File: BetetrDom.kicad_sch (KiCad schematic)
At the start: 8 parts, among them J1 XT60PW-M, J2 Raspberry_Pi_2_3

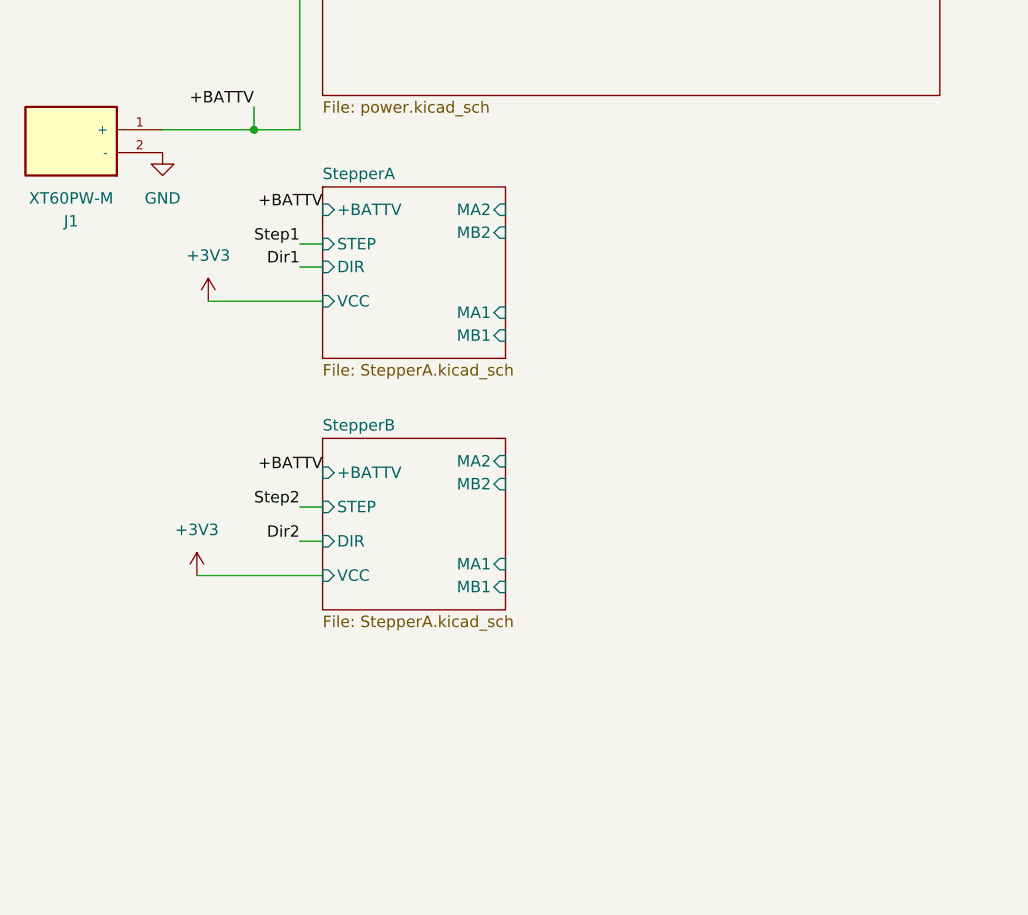
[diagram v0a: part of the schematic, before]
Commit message: with ports for steppers
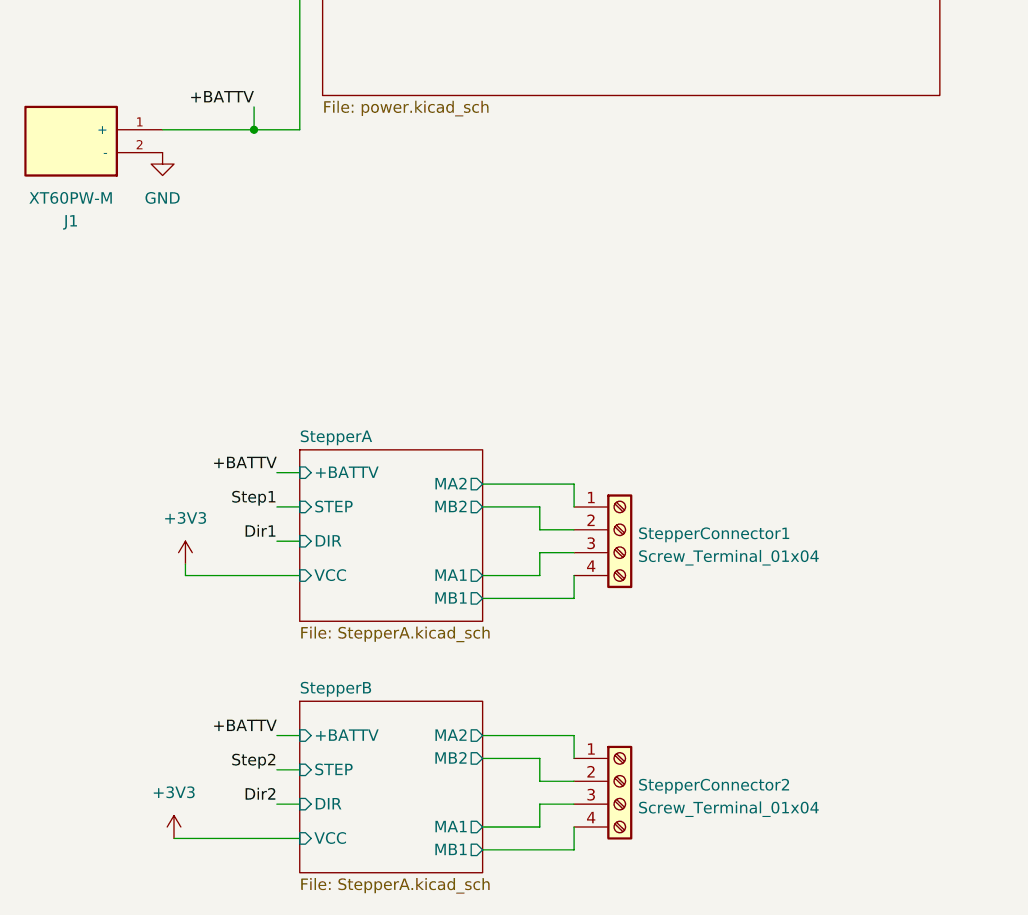
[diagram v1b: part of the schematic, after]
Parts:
- added StepperConnector1, StepperConnector2: Screw_Terminal_01x04, TerminalBlock_TE-Connectivity:TerminalBlock_TE_282834-4_1x04_P2.54mm_Horizontal, symbol Connector:Screw_Terminal_01x04
- J1: footprint AMASS_XT60PW-M -> iclr:AMASS_XT60PW-M
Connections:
- net StepperA/MA1: now also StepperConnector1.3 (Pin_3)
- net StepperA/MA2: now also StepperConnector1.1 (Pin_1)
- net StepperA/MB1: now also StepperConnector1.4 (Pin_4)
- net StepperA/MB2: now also StepperConnector1.2 (Pin_2)
- net StepperB/MA1: now also StepperConnector2.3 (Pin_3)
- net StepperB/MA2: now also StepperConnector2.1 (Pin_1)
- net StepperB/MB1: now also StepperConnector2.4 (Pin_4)
- net StepperB/MB2: now also StepperConnector2.2 (Pin_2)

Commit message: added zener diodes
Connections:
- net ID_SCL_EEPROM: no longer names the net of J2.28 (ID_SC/GPIO1)
- net ID_SCL_EEPROM: now also J2.27 (ID_SD/GPIO0); no longer TP6.1
- net ID_SDA_EEPROM: no longer names the net of TP5.1
- net ID_SDA_EEPROM: no longer J2.27 (ID_SD/GPIO0)
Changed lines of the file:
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@@
+	(wire
+		(pts
+			(xy 194.31 77.47) (xy 194.31 80.01)
+		)
+		(stroke
+			(width 0)
+			(type default)
+		)
+	)
 	(wire
 		(pts
@@
 	(wire
 		(pts
-			(xy 194.31 77.47) (xy 213.36 77.47)
-		)
-		(stroke
-			(width 0)
-			(type default)
-		)
-	)
-	(wire
-		(pts
 			(xy 177.8 67.31) (xy 179.07 67.31)
 		)
@@
 	(wire
 		(pts
-			(xy 194.31 80.01) (xy 213.36 80.01)
-		)
-		(stroke
-			(width 0)
-			(type default)
-		)
-	)
-	(wire
-		(pts
 			(xy 73.66 104.14) (xy 77.47 104.14)
 		)
@@
 			(width 0)
 			(type default)
-		)
-	)
-	(label "ID_SCL_EEPROM"
-		(at 196.85 80.01 0)
-		(fields_autoplaced yes)
-		(effects
-			(font
-				(size 1.27 1.27)
-			)
-			(justify left bottom)
 		)
 	)
@@
 		)
 	)
-	(label "ID_SDA_EEPROM"
-		(at 196.85 77.47 0)
-		(fields_autoplaced yes)
-		(effects
-			(font
-				(size 1.27 1.27)
-			)
-			(justify left bottom)
-		)
-	)

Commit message: UPDATE
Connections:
- net at J2.27 (ID_SD/GPIO0), J2.28 (ID_SC/GPIO1): now also TP5.1, TP6.1
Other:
- moved on the sheet: TP5, TP6
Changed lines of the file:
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@@
 	(paper "A4")
+	(junction
+		(at 194.31 77.47)
+		(diameter 0)
+		(color 0 0 0 0)
+	)
 	(junction
 		(at 179.07 133.35)
@@
 	(junction
 		(at 41.91 59.69)
+		(diameter 0)
+		(color 0 0 0 0)
+	)
+	(junction
+		(at 194.31 80.01)
 		(diameter 0)
 		(color 0 0 0 0)
@@
 	(symbol
 		(lib_id "Connector:TestPoint")
-		(at 213.36 80.01 270)
+		(at 194.31 80.01 270)
 		(unit 1)
 		(exclude_from_sim no)
@@
 		(fields_autoplaced yes)
 		(property "Reference" "TP6"
-			(at 218.059 79.1753 90)
+			(at 199.009 79.1753 90)
 			(effects
 				(font
@@
 		)
 		(property "Value" "SCL_EEPROM"
-			(at 218.059 81.7122 90)
+			(at 199.009 81.7122 90)
 			(effects
 				(font
@@
 		)
 		(property "Footprint" "TestPoint:TestPoint_Pad_1.5x1.5mm"
-			(at 213.36 85.09 0)
+			(at 194.31 85.09 0)
 			(effects
 				(font
@@
 		)
 		(property "Datasheet" "~"
-			(at 213.36 85.09 0)
+			(at 194.31 85.09 0)
 			(effects
 				(font
@@
 		)
 		(property "Description" ""
-			(at 213.36 80.01 0)
+			(at 194.31 80.01 0)
 			(effects
 				(font
@@
 	(symbol
 		(lib_id "Connector:TestPoint")
-		(at 213.36 77.47 270)
+		(at 194.31 77.47 270)
 		(unit 1)
 		(exclude_from_sim no)
@@
 		(fields_autoplaced yes)
 		(property "Reference" "TP5"
-			(at 218.059 76.6353 90)
+			(at 199.009 76.6353 90)
 			(effects
 				(font
@@
 		)
 		(property "Value" "SDA_EEPROM"
-			(at 218.059 79.1722 90)
+			(at 199.009 79.1722 90)
 			(effects
 				(font
@@
 		)
 		(property "Footprint" "TestPoint:TestPoint_Pad_1.5x1.5mm"
-			(at 213.36 82.55 0)
+			(at 194.31 82.55 0)
 			(effects
 				(font
@@
 		)
 		(property "Datasheet" "~"
-			(at 213.36 82.55 0)
+			(at 194.31 82.55 0)
 			(effects
 				(font
@@
 		)
 		(property "Description" ""
-			(at 213.36 77.47 0)
-			(effects
-				(font
+			(at 194.31 77.47 0)
+			(effects
+				(font

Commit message: finished pcb layouts, ready for check p sure
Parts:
- added C5: 0.1uF, Capacitor_SMD:C_0402_1005Metric, symbol Device:C_Small
- added H1, H2, H3, H4: MountingHole_Pad, MountingHole:MountingHole_3.2mm_M3_DIN965_Pad, symbol Mechanical:MountingHole_Pad
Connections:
- net GND: now also C5.2, H1.1, H2.1, H3.1, H4.1; no longer J1.2 (-)
- net StepperA/MA1: now also StepperConnector1.2 (Pin_2); no longer StepperConnector1.3 (Pin_3)
- net StepperA/MB1: now also StepperConnector1.3 (Pin_3); no longer StepperConnector1.4 (Pin_4)
- net StepperA/MB2: now also StepperConnector1.4 (Pin_4); no longer StepperConnector1.2 (Pin_2)
- net StepperB/MA1: now also StepperConnector2.2 (Pin_2); no longer StepperConnector2.3 (Pin_3)
- net StepperB/MB1: now also StepperConnector2.3 (Pin_3); no longer StepperConnector2.4 (Pin_4)
- net StepperB/MB2: now also StepperConnector2.4 (Pin_4); no longer StepperConnector2.2 (Pin_2)
- net +BATTV renamed power/+BATTV
- new net: C5.1, J1.2 (-)
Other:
- sheet StepperA ports: added VMAIN; removed +BATTV
- sheet StepperB ports: added VMAIN; removed +BATTV
- sheet power ports: added VMAIN; removed none

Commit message: update
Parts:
- removed TP5: SDA_EEPROM, TestPoint:TestPoint_Pad_1.5x1.5mm, symbol Connector:TestPoint
- removed TP6: SCL_EEPROM, TestPoint:TestPoint_Pad_1.5x1.5mm, symbol Connector:TestPoint
- StepperConnector1, StepperConnector2: footprint TerminalBlock_TE-Connectivity:TerminalBlock_TE_282834-4_1x04_P2.54mm_Horizontal -> Connector_Molex:Molex_Nano-Fit_105313-xx04_1x04_P2.50mm_Horizontal
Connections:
- net at J2.27 (ID_SD/GPIO0): no longer J2.28 (ID_SC/GPIO1)
- no-connect marks 22 -> 24
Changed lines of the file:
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@@
 	(paper "A4")
-	(junction
-		(at 194.31 77.47)
-		(diameter 0)
-		(color 0 0 0 0)
-	)
 	(junction
 		(at 233.68 90.17)
@@
 	)
 	(junction
-		(at 194.31 80.01)
-		(diameter 0)
-		(color 0 0 0 0)
-	)
-	(junction
 		(at 166.37 133.35)
 		(diameter 0)
@@
 	)
 	(no_connect
+		(at 194.31 80.01)
+	)
+	(no_connect
+		(at 194.31 77.47)
+	)
+	(no_connect
 		(at 194.31 92.71)
 	)
@@
 		(pts
 			(xy 69.85 130.81) (xy 67.31 130.81)
-		)
-		(stroke
-			(width 0)
-			(type default)
-		)
-	)
-	(wire
-		(pts
-			(xy 194.31 77.47) (xy 194.31 80.01)
 		)
 		(stroke
@@
 	)
 	(symbol
-		(lib_id "Connector:TestPoint")
-		(at 194.31 80.01 270)
-		(unit 1)
-		(exclude_from_sim no)
-		(in_bom yes)
-		(on_board yes)
-		(dnp no)
-		(fields_autoplaced yes)
-		(property "Reference" "TP6"
-			(at 199.009 79.1753 90)
-			(effects
-				(font
-					(size 1.27 1.27)
-				)
-				(justify left)
-			)
-		)
-		(property "Value" "SCL_EEPROM"
-			(at 199.009 81.7122 90)
-			(effects
-				(font
-					(size 1.27 1.27)
-				)
-				(justify left)
-			)
-		)
-		(property "Footprint" "TestPoint:TestPoint_Pad_1.5x1.5mm"
-			(at 194.31 85.09 0)
-			(effects
-				(font
-					(size 1.27 1.27)
-				)
-				(hide yes)
-			)
-		)
-		(property "Datasheet" "~"
-			(at 194.31 85.09 0)
-			(effects
-				(font
-					(size 1.27 1.27)
-				)
-				(hide yes)
-			)
-		)
-		(property "Description" ""
-			(at 194.31 80.01 0)
-			(effects
-				(font
-					(size 1.27 1.27)
-				)
-				(hide yes)
-			)
-		)
-		(pin "1"
-		)
-		(instances
-			(project "BetetrDom"
-				(path "/3d73b00f-865e-402b-88ef-ae22e0a8ba36"
-					(reference "TP6")
-					(unit 1)
-				)
-			)
-		)
-	)
-	(symbol
 		(lib_id "Connector:Screw_Terminal_01x04")
 		(at 82.55 104.14 0)
@@
 			)
 		)
-		(property "Footprint" "TerminalBlock_TE-Connectivity:TerminalBlock_TE_282834-4_1x04_P2.54mm_Horizontal"
+		(property "Footprint" "Connector_Molex:Molex_Nano-Fit_105313-xx04_1x04_P2.50mm_Horizontal"
 			(at 82.55 104.14 0)
 			(effects
@@
 			)
 		)
-		(property "Footprint" "TerminalBlock_TE-Connectivity:TerminalBlock_TE_282834-4_1x04_P2.54mm_Horizontal"
+		(property "Footprint" "Connector_Molex:Molex_Nano-Fit_105313-xx04_1x04_P2.50mm_Horizontal"
 			(at 82.55 132.08 0)
 			(effects
@@
 					(unit 1)
 				)
-			)
-		)
-	)
-	(symbol
-		(lib_id "Connector:TestPoint")
-		(at 194.31 77.47 270)
-		(unit 1)
-		(exclude_from_sim no)
-		(in_bom yes)
-		(on_board yes)
-		(dnp no)
-		(fields_autoplaced yes)
-		(property "Reference" "TP5"
-			(at 199.009 76.6353 90)
-			(effects
-				(font
-					(size 1.27 1.27)
-				)
-				(justify left)
-			)
-		)
-		(property "Value" "SDA_EEPROM"
-			(at 199.009 79.1722 90)
-			(effects
-				(font
-					(size 1.27 1.27)
-				)
-				(justify left)
-			)
-		)
-		(property "Footprint" "TestPoint:TestPoint_Pad_1.5x1.5mm"
-			(at 194.31 82.55 0)
-			(effects
-				(font
-					(size 1.27 1.27)
-				)
-				(hide yes)
-			)
-		)
-		(property "Datasheet" "~"
-			(at 194.31 82.55 0)
-			(effects
-				(font
-					(size 1.27 1.27)
-				)
-				(hide yes)
-			)
-		)
-		(property "Description" ""
-			(at 194.31 77.47 0)
-			(effects
-				(font
-					(size 1.27 1.27)
-				)
-				(hide yes)
-			)
-		)
-		(pin "1"
-		)
-		(instances
-			(project "BetetrDom"
-				(path "/3d73b00f-865e-402b-88ef-ae22e0a8ba36"
-					(reference "TP5")
-					(unit 1)
-				)
